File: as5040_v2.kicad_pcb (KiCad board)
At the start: 2 copper layers, 28 x 28 mm, 22 parts, among them J1 Conn_02x05_Odd_Even, J2 Conn_01x05_Male, J3 Conn_01x06_Male, J4 Conn_01x03_Male, U1 AS5045B

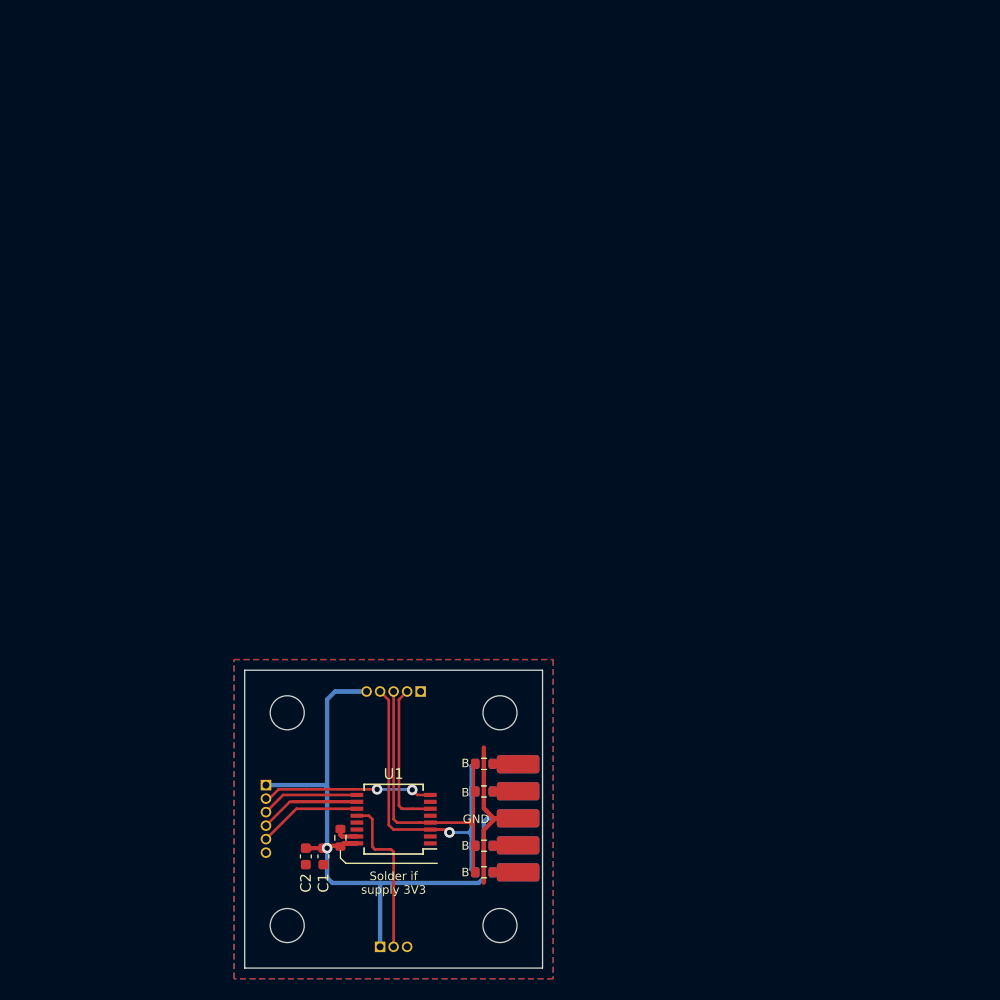
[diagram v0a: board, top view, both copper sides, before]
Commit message: 3x3 grid for cheap pcb production
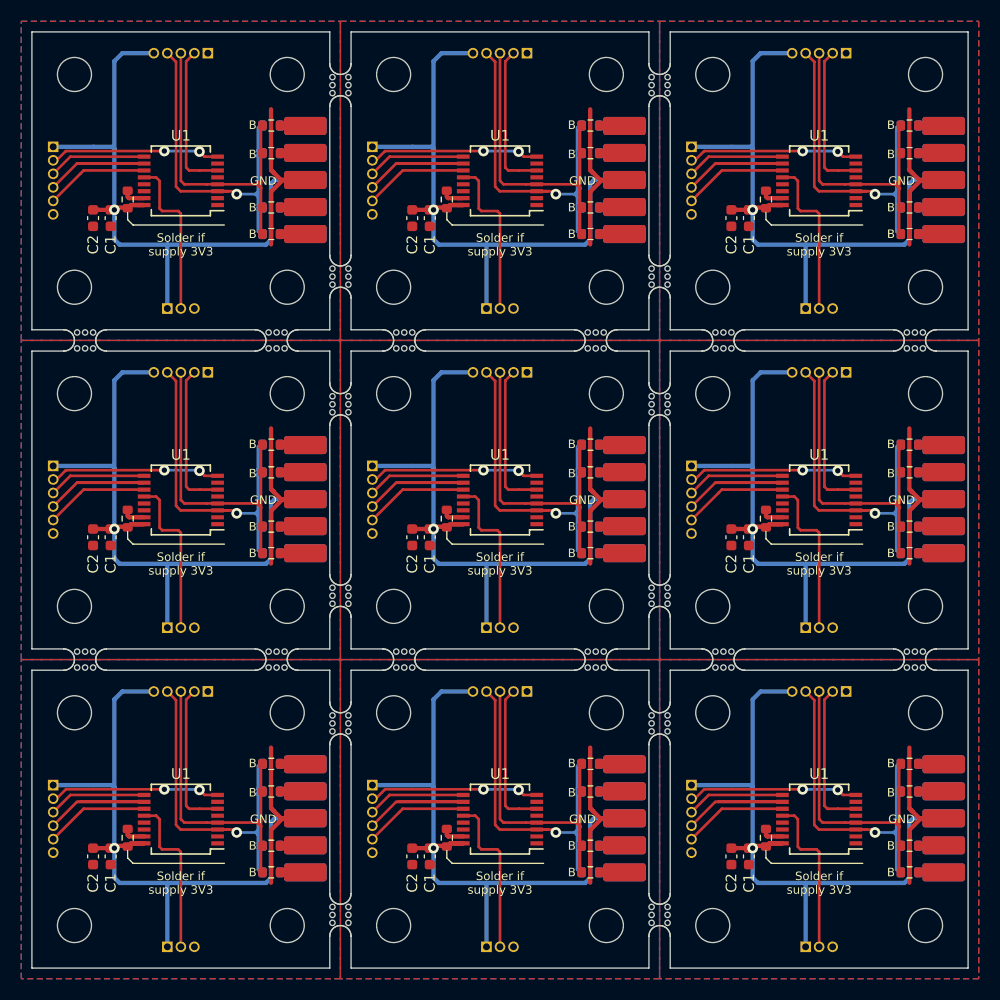
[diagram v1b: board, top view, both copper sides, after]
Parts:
- removed the C1 at (97.4, 139.5)
- removed the C2 at (95.8, 139.5)
- removed the J1 at (113.5, 141.0)
- removed the J2 at (106.5, 124.0)
- removed the J3 at (92.0, 132.8)
- removed the J4 at (102.7, 148.0)
- removed the R1 at (112.5, 133.4)
- removed the R2 at (112.5, 141.0)
- removed the R3 at (112.5, 130.8)
- removed the R4 at (112.5, 138.5)
- removed the R5 at (112.5, 138.5)
- removed the R6 at (112.5, 141.0)
- removed the R7 at (112.5, 130.8)
- removed the R8 at (112.5, 133.4)
- removed the R9 at (99.0, 137.8)
- removed the REF** at (114.0, 146.0)
- removed the REF** at (114.0, 126.0)
- removed the U1 at (104.0, 136.0)
- added C1: 0.1uF, Capacitor_SMD:C_0603_1608Metric, F.Cu at (137.4, 139.5)
- added C1: 0.1uF, Capacitor_SMD:C_0603_1608Metric, F.Cu at (137.4, 79.5)
- added C1: 0.1uF, Capacitor_SMD:C_0603_1608Metric, F.Cu at (137.4, 109.5)
- added C1: 0.1uF, Capacitor_SMD:C_0603_1608Metric, F.Cu at (107.4, 139.5)
- added C1: 0.1uF, Capacitor_SMD:C_0603_1608Metric, F.Cu at (107.4, 79.5)
- added C1: 0.1uF, Capacitor_SMD:C_0603_1608Metric, F.Cu at (107.4, 109.5)
- added C1: 0.1uF, Capacitor_SMD:C_0603_1608Metric, F.Cu at (77.4, 79.5)
- added C1: 0.1uF, Capacitor_SMD:C_0603_1608Metric, F.Cu at (77.4, 109.5)
- added C1: 0.1uF, Capacitor_SMD:C_0603_1608Metric, F.Cu at (77.4, 139.5)
- added C2: 1uF, Capacitor_SMD:C_0603_1608Metric, F.Cu at (135.8, 109.5)
- added C2: 1uF, Capacitor_SMD:C_0603_1608Metric, F.Cu at (135.8, 79.5)
- added C2: 1uF, Capacitor_SMD:C_0603_1608Metric, F.Cu at (135.8, 139.5)
- added C2: 1uF, Capacitor_SMD:C_0603_1608Metric, F.Cu at (105.8, 109.5)
- added C2: 1uF, Capacitor_SMD:C_0603_1608Metric, F.Cu at (105.8, 79.5)
- added C2: 1uF, Capacitor_SMD:C_0603_1608Metric, F.Cu at (105.8, 139.5)
- added C2: 1uF, Capacitor_SMD:C_0603_1608Metric, F.Cu at (75.8, 79.5)
- added C2: 1uF, Capacitor_SMD:C_0603_1608Metric, F.Cu at (75.8, 109.5)
- added C2: 1uF, Capacitor_SMD:C_0603_1608Metric, F.Cu at (75.8, 139.5)
- added G***: LOGO, graphics:progresja_13.4x3.8mm, B.Cu at (143.0, 130.5)
- added G***: LOGO, graphics:progresja_13.4x3.8mm, B.Cu at (143.0, 100.5)
- added G***: LOGO, graphics:progresja_13.4x3.8mm, B.Cu at (143.0, 70.5)
- added G***: LOGO, graphics:progresja_13.4x3.8mm, B.Cu at (113.0, 130.5)
- added G***: LOGO, graphics:progresja_13.4x3.8mm, B.Cu at (113.0, 100.5)
- added G***: LOGO, graphics:progresja_13.4x3.8mm, B.Cu at (113.0, 70.5)
- added G***: LOGO, graphics:progresja_13.4x3.8mm, B.Cu at (83.0, 70.5)
- added G***: LOGO, graphics:progresja_13.4x3.8mm, B.Cu at (83.0, 100.5)
- added J1: Conn_02x05_Odd_Even, as5040_v2:IDC-Header_2x05_P2.54mm_Horizontal, B.Cu at (153.5, 141.0)
- added J1: Conn_02x05_Odd_Even, as5040_v2:IDC-Header_2x05_P2.54mm_Horizontal, B.Cu at (153.5, 111.0)
- added J1: Conn_02x05_Odd_Even, as5040_v2:IDC-Header_2x05_P2.54mm_Horizontal, B.Cu at (153.5, 81.0)
- added J1: Conn_02x05_Odd_Even, as5040_v2:IDC-Header_2x05_P2.54mm_Horizontal, B.Cu at (123.5, 141.0)
- added J1: Conn_02x05_Odd_Even, as5040_v2:IDC-Header_2x05_P2.54mm_Horizontal, B.Cu at (123.5, 111.0)
- added J1: Conn_02x05_Odd_Even, as5040_v2:IDC-Header_2x05_P2.54mm_Horizontal, B.Cu at (123.5, 81.0)
- added J1: Conn_02x05_Odd_Even, as5040_v2:IDC-Header_2x05_P2.54mm_Horizontal, B.Cu at (93.5, 81.0)
- added J1: Conn_02x05_Odd_Even, as5040_v2:IDC-Header_2x05_P2.54mm_Horizontal, B.Cu at (93.5, 111.0)
- added J1: Conn_02x05_Odd_Even, as5040_v2:IDC-Header_2x05_P2.54mm_Horizontal, B.Cu at (93.5, 141.0)
- added J2: Conn_01x05_Male, as5040_v2:PinHeader_1x05_P1.27mm_Horizontal, B.Cu at (146.5, 64.0)
- added J2: Conn_01x05_Male, as5040_v2:PinHeader_1x05_P1.27mm_Horizontal, B.Cu at (146.5, 94.0)
- added J2: Conn_01x05_Male, as5040_v2:PinHeader_1x05_P1.27mm_Horizontal, B.Cu at (146.5, 124.0)
- added J2: Conn_01x05_Male, as5040_v2:PinHeader_1x05_P1.27mm_Horizontal, B.Cu at (116.5, 64.0)
- added J2: Conn_01x05_Male, as5040_v2:PinHeader_1x05_P1.27mm_Horizontal, B.Cu at (116.5, 94.0)
- added J2: Conn_01x05_Male, as5040_v2:PinHeader_1x05_P1.27mm_Horizontal, B.Cu at (116.5, 124.0)
- added J2: Conn_01x05_Male, as5040_v2:PinHeader_1x05_P1.27mm_Horizontal, B.Cu at (86.5, 64.0)
- added J2: Conn_01x05_Male, as5040_v2:PinHeader_1x05_P1.27mm_Horizontal, B.Cu at (86.5, 94.0)
- added J2: Conn_01x05_Male, as5040_v2:PinHeader_1x05_P1.27mm_Horizontal, B.Cu at (86.5, 124.0)
- added J3: Conn_01x06_Male, as5040_v2:PinHeader_1x06_P1.27mm_Horizontal, B.Cu at (132.0, 102.8)
- added J3: Conn_01x06_Male, as5040_v2:PinHeader_1x06_P1.27mm_Horizontal, B.Cu at (132.0, 132.8)
- added J3: Conn_01x06_Male, as5040_v2:PinHeader_1x06_P1.27mm_Horizontal, B.Cu at (132.0, 72.8)
- added J3: Conn_01x06_Male, as5040_v2:PinHeader_1x06_P1.27mm_Horizontal, B.Cu at (102.0, 102.8)
- added J3: Conn_01x06_Male, as5040_v2:PinHeader_1x06_P1.27mm_Horizontal, B.Cu at (102.0, 132.8)
- added J3: Conn_01x06_Male, as5040_v2:PinHeader_1x06_P1.27mm_Horizontal, B.Cu at (102.0, 72.8)
- added J3: Conn_01x06_Male, as5040_v2:PinHeader_1x06_P1.27mm_Horizontal, B.Cu at (72.0, 72.8)
- added J3: Conn_01x06_Male, as5040_v2:PinHeader_1x06_P1.27mm_Horizontal, B.Cu at (72.0, 102.8)
- added J3: Conn_01x06_Male, as5040_v2:PinHeader_1x06_P1.27mm_Horizontal, B.Cu at (72.0, 132.8)
- added J4: Conn_01x03_Male, as5040_v2:PinHeader_1x03_P1.27mm_Horizontal, B.Cu at (142.7, 148.0)
- added J4: Conn_01x03_Male, as5040_v2:PinHeader_1x03_P1.27mm_Horizontal, B.Cu at (142.7, 88.0)
- added J4: Conn_01x03_Male, as5040_v2:PinHeader_1x03_P1.27mm_Horizontal, B.Cu at (142.7, 118.0)
- added J4: Conn_01x03_Male, as5040_v2:PinHeader_1x03_P1.27mm_Horizontal, B.Cu at (112.7, 148.0)
- added J4: Conn_01x03_Male, as5040_v2:PinHeader_1x03_P1.27mm_Horizontal, B.Cu at (112.7, 88.0)
- added J4: Conn_01x03_Male, as5040_v2:PinHeader_1x03_P1.27mm_Horizontal, B.Cu at (112.7, 118.0)
- added J4: Conn_01x03_Male, as5040_v2:PinHeader_1x03_P1.27mm_Horizontal, B.Cu at (82.7, 88.0)
- added J4: Conn_01x03_Male, as5040_v2:PinHeader_1x03_P1.27mm_Horizontal, B.Cu at (82.7, 118.0)
- added J4: Conn_01x03_Male, as5040_v2:PinHeader_1x03_P1.27mm_Horizontal, B.Cu at (82.7, 148.0)
- added R1: 0R, Resistor_SMD:R_0603_1608Metric, B.Cu at (152.5, 103.4)
- added R1: 0R, Resistor_SMD:R_0603_1608Metric, B.Cu at (152.5, 133.4)
- added R1: 0R, Resistor_SMD:R_0603_1608Metric, B.Cu at (152.5, 73.4)
- added R1: 0R, Resistor_SMD:R_0603_1608Metric, B.Cu at (122.5, 103.4)
- added R1: 0R, Resistor_SMD:R_0603_1608Metric, B.Cu at (122.5, 133.4)
- added R1: 0R, Resistor_SMD:R_0603_1608Metric, B.Cu at (122.5, 73.4)
- added R1: 0R, Resistor_SMD:R_0603_1608Metric, B.Cu at (92.5, 73.4)
- added R1: 0R, Resistor_SMD:R_0603_1608Metric, B.Cu at (92.5, 103.4)
- added R1: 0R, Resistor_SMD:R_0603_1608Metric, B.Cu at (92.5, 133.4)
- added R2: 0R, Resistor_SMD:R_0603_1608Metric, B.Cu at (152.5, 141.0)
- added R2: 0R, Resistor_SMD:R_0603_1608Metric, B.Cu at (152.5, 111.0)
- added R2: 0R, Resistor_SMD:R_0603_1608Metric, B.Cu at (152.5, 81.0)
- added R2: 0R, Resistor_SMD:R_0603_1608Metric, B.Cu at (122.5, 141.0)
- added R2: 0R, Resistor_SMD:R_0603_1608Metric, B.Cu at (122.5, 111.0)
- added R2: 0R, Resistor_SMD:R_0603_1608Metric, B.Cu at (122.5, 81.0)
- added R2: 0R, Resistor_SMD:R_0603_1608Metric, B.Cu at (92.5, 81.0)
- added R2: 0R, Resistor_SMD:R_0603_1608Metric, B.Cu at (92.5, 111.0)
- added R2: 0R, Resistor_SMD:R_0603_1608Metric, B.Cu at (92.5, 141.0)
- added R3: 0R, Resistor_SMD:R_0603_1608Metric, B.Cu at (152.5, 130.8)
- added R3: 0R, Resistor_SMD:R_0603_1608Metric, B.Cu at (152.5, 70.8)
- added R3: 0R, Resistor_SMD:R_0603_1608Metric, B.Cu at (152.5, 100.8)
- added R3: 0R, Resistor_SMD:R_0603_1608Metric, B.Cu at (122.5, 130.8)
- added R3: 0R, Resistor_SMD:R_0603_1608Metric, B.Cu at (122.5, 70.8)
- added R3: 0R, Resistor_SMD:R_0603_1608Metric, B.Cu at (122.5, 100.8)
- added R3: 0R, Resistor_SMD:R_0603_1608Metric, B.Cu at (92.5, 70.8)
- added R3: 0R, Resistor_SMD:R_0603_1608Metric, B.Cu at (92.5, 100.8)
- added R3: 0R, Resistor_SMD:R_0603_1608Metric, B.Cu at (92.5, 130.8)
- added R4: 0R, Resistor_SMD:R_0603_1608Metric, B.Cu at (152.5, 78.5)
- added R4: 0R, Resistor_SMD:R_0603_1608Metric, B.Cu at (152.5, 138.5)
- added R4: 0R, Resistor_SMD:R_0603_1608Metric, B.Cu at (152.5, 108.5)
- added R4: 0R, Resistor_SMD:R_0603_1608Metric, B.Cu at (122.5, 78.5)
- added R4: 0R, Resistor_SMD:R_0603_1608Metric, B.Cu at (122.5, 138.5)
- added R4: 0R, Resistor_SMD:R_0603_1608Metric, B.Cu at (122.5, 108.5)
- added R4: 0R, Resistor_SMD:R_0603_1608Metric, B.Cu at (92.5, 78.5)
- added R4: 0R, Resistor_SMD:R_0603_1608Metric, B.Cu at (92.5, 108.5)
- added R4: 0R, Resistor_SMD:R_0603_1608Metric, B.Cu at (92.5, 138.5)
- added R5: 0R, Resistor_SMD:R_0603_1608Metric, F.Cu at (152.5, 138.5)
- added R5: 0R, Resistor_SMD:R_0603_1608Metric, F.Cu at (152.5, 108.5)
- added R5: 0R, Resistor_SMD:R_0603_1608Metric, F.Cu at (152.5, 78.5)
- added R5: 0R, Resistor_SMD:R_0603_1608Metric, F.Cu at (122.5, 138.5)
- added R5: 0R, Resistor_SMD:R_0603_1608Metric, F.Cu at (122.5, 108.5)
- added R5: 0R, Resistor_SMD:R_0603_1608Metric, F.Cu at (122.5, 78.5)
- added R5: 0R, Resistor_SMD:R_0603_1608Metric, F.Cu at (92.5, 78.5)
- added R5: 0R, Resistor_SMD:R_0603_1608Metric, F.Cu at (92.5, 108.5)
- added R5: 0R, Resistor_SMD:R_0603_1608Metric, F.Cu at (92.5, 138.5)
- added R6: 0R, Resistor_SMD:R_0603_1608Metric, F.Cu at (152.5, 141.0)
- added R6: 0R, Resistor_SMD:R_0603_1608Metric, F.Cu at (152.5, 111.0)
- added R6: 0R, Resistor_SMD:R_0603_1608Metric, F.Cu at (152.5, 81.0)
- added R6: 0R, Resistor_SMD:R_0603_1608Metric, F.Cu at (122.5, 141.0)
- added R6: 0R, Resistor_SMD:R_0603_1608Metric, F.Cu at (122.5, 111.0)
- added R6: 0R, Resistor_SMD:R_0603_1608Metric, F.Cu at (122.5, 81.0)
- added R6: 0R, Resistor_SMD:R_0603_1608Metric, F.Cu at (92.5, 81.0)
- added R6: 0R, Resistor_SMD:R_0603_1608Metric, F.Cu at (92.5, 111.0)
- added R6: 0R, Resistor_SMD:R_0603_1608Metric, F.Cu at (92.5, 141.0)
- added R7: 0R, Resistor_SMD:R_0603_1608Metric, F.Cu at (152.5, 130.8)
- added R7: 0R, Resistor_SMD:R_0603_1608Metric, F.Cu at (152.5, 100.8)
- added R7: 0R, Resistor_SMD:R_0603_1608Metric, F.Cu at (152.5, 70.8)
- added R7: 0R, Resistor_SMD:R_0603_1608Metric, F.Cu at (122.5, 130.8)
- added R7: 0R, Resistor_SMD:R_0603_1608Metric, F.Cu at (122.5, 100.8)
- added R7: 0R, Resistor_SMD:R_0603_1608Metric, F.Cu at (122.5, 70.8)
- added R7: 0R, Resistor_SMD:R_0603_1608Metric, F.Cu at (92.5, 70.8)
- added R7: 0R, Resistor_SMD:R_0603_1608Metric, F.Cu at (92.5, 100.8)
- added R7: 0R, Resistor_SMD:R_0603_1608Metric, F.Cu at (92.5, 130.8)
- added R8: 0R, Resistor_SMD:R_0603_1608Metric, F.Cu at (152.5, 103.4)
- added R8: 0R, Resistor_SMD:R_0603_1608Metric, F.Cu at (152.5, 133.4)
- added R8: 0R, Resistor_SMD:R_0603_1608Metric, F.Cu at (152.5, 73.4)
- added R8: 0R, Resistor_SMD:R_0603_1608Metric, F.Cu at (122.5, 103.4)
- added R8: 0R, Resistor_SMD:R_0603_1608Metric, F.Cu at (122.5, 133.4)
- added R8: 0R, Resistor_SMD:R_0603_1608Metric, F.Cu at (122.5, 73.4)
- added R8: 0R, Resistor_SMD:R_0603_1608Metric, F.Cu at (92.5, 73.4)
- added R8: 0R, Resistor_SMD:R_0603_1608Metric, F.Cu at (92.5, 103.4)
- added R8: 0R, Resistor_SMD:R_0603_1608Metric, F.Cu at (92.5, 133.4)
- added R9: 0R, Resistor_SMD:R_0603_1608Metric, F.Cu at (139.0, 107.8)
- added R9: 0R, Resistor_SMD:R_0603_1608Metric, F.Cu at (139.0, 137.8)
- added R9: 0R, Resistor_SMD:R_0603_1608Metric, F.Cu at (139.0, 77.8)
- added R9: 0R, Resistor_SMD:R_0603_1608Metric, F.Cu at (109.0, 107.8)
- added R9: 0R, Resistor_SMD:R_0603_1608Metric, F.Cu at (109.0, 137.8)
- added R9: 0R, Resistor_SMD:R_0603_1608Metric, F.Cu at (109.0, 77.8)
- added R9: 0R, Resistor_SMD:R_0603_1608Metric, F.Cu at (79.0, 77.8)
- added R9: 0R, Resistor_SMD:R_0603_1608Metric, F.Cu at (79.0, 107.8)
- added R9: 0R, Resistor_SMD:R_0603_1608Metric, F.Cu at (79.0, 137.8)
- added REF**: OSHW-Logo_5.7x6mm_SilkScreen, Symbol:OSHW-Logo_5.7x6mm_SilkScreen, B.Cu at (140.0, 140.5)
- added REF**: MountingHole_3.2mm_M3, MountingHole:MountingHole_3.2mm_M3, F.Cu at (134.0, 86.0)
- added REF**: MountingHole_3.2mm_M3, MountingHole:MountingHole_3.2mm_M3, F.Cu at (154.0, 96.0)
- added REF**: MountingHole_3.2mm_M3, MountingHole:MountingHole_3.2mm_M3, F.Cu at (134.0, 116.0)
- added REF**: MountingHole_3.2mm_M3, MountingHole:MountingHole_3.2mm_M3, F.Cu at (154.0, 116.0)
- added REF**: OSHW-Logo_5.7x6mm_SilkScreen, Symbol:OSHW-Logo_5.7x6mm_SilkScreen, B.Cu at (140.0, 110.5)
- added REF**: MountingHole_3.2mm_M3, MountingHole:MountingHole_3.2mm_M3, F.Cu at (154.0, 86.0)
- added REF**: OSHW-Logo_5.7x6mm_SilkScreen, Symbol:OSHW-Logo_5.7x6mm_SilkScreen, B.Cu at (110.0, 140.5)
- added REF**: MountingHole_3.2mm_M3, MountingHole:MountingHole_3.2mm_M3, F.Cu at (104.0, 96.0)
- added REF**: MountingHole_3.2mm_M3, MountingHole:MountingHole_3.2mm_M3, F.Cu at (124.0, 126.0)
- added REF**: MountingHole_3.2mm_M3, MountingHole:MountingHole_3.2mm_M3, F.Cu at (104.0, 126.0)
- added REF**: MountingHole_3.2mm_M3, MountingHole:MountingHole_3.2mm_M3, F.Cu at (134.0, 96.0)
- added REF**: MountingHole_3.2mm_M3, MountingHole:MountingHole_3.2mm_M3, F.Cu at (124.0, 146.0)
- added REF**: MountingHole_3.2mm_M3, MountingHole:MountingHole_3.2mm_M3, F.Cu at (104.0, 146.0)
- added REF**: MountingHole_3.2mm_M3, MountingHole:MountingHole_3.2mm_M3, F.Cu at (124.0, 66.0)
- added REF**: MountingHole_3.2mm_M3, MountingHole:MountingHole_3.2mm_M3, F.Cu at (104.0, 66.0)
- added REF**: OSHW-Logo_5.7x6mm_SilkScreen, Symbol:OSHW-Logo_5.7x6mm_SilkScreen, B.Cu at (110.0, 80.5)
- added REF**: MountingHole_3.2mm_M3, MountingHole:MountingHole_3.2mm_M3, F.Cu at (104.0, 86.0)
- added REF**: MountingHole_3.2mm_M3, MountingHole:MountingHole_3.2mm_M3, F.Cu at (124.0, 96.0)
- added REF**: MountingHole_3.2mm_M3, MountingHole:MountingHole_3.2mm_M3, F.Cu at (104.0, 116.0)
- added REF**: MountingHole_3.2mm_M3, MountingHole:MountingHole_3.2mm_M3, F.Cu at (124.0, 116.0)
- added REF**: OSHW-Logo_5.7x6mm_SilkScreen, Symbol:OSHW-Logo_5.7x6mm_SilkScreen, B.Cu at (110.0, 110.5)
- added REF**: MountingHole_3.2mm_M3, MountingHole:MountingHole_3.2mm_M3, F.Cu at (154.0, 126.0)
- added REF**: MountingHole_3.2mm_M3, MountingHole:MountingHole_3.2mm_M3, F.Cu at (124.0, 86.0)
- added REF**: OSHW-Logo_5.7x6mm_SilkScreen, Symbol:OSHW-Logo_5.7x6mm_SilkScreen, B.Cu at (80.0, 80.5)
- added REF**: MountingHole_3.2mm_M3, MountingHole:MountingHole_3.2mm_M3, F.Cu at (94.0, 66.0)
- added REF**: MountingHole_3.2mm_M3, MountingHole:MountingHole_3.2mm_M3, F.Cu at (74.0, 66.0)
- added REF**: MountingHole_3.2mm_M3, MountingHole:MountingHole_3.2mm_M3, F.Cu at (94.0, 86.0)
- added REF**: MountingHole_3.2mm_M3, MountingHole:MountingHole_3.2mm_M3, F.Cu at (74.0, 86.0)
- added REF**: OSHW-Logo_5.7x6mm_SilkScreen, Symbol:OSHW-Logo_5.7x6mm_SilkScreen, B.Cu at (80.0, 110.5)
- added REF**: MountingHole_3.2mm_M3, MountingHole:MountingHole_3.2mm_M3, F.Cu at (94.0, 96.0)
- added REF**: MountingHole_3.2mm_M3, MountingHole:MountingHole_3.2mm_M3, F.Cu at (74.0, 96.0)
- added REF**: MountingHole_3.2mm_M3, MountingHole:MountingHole_3.2mm_M3, F.Cu at (94.0, 116.0)
- added REF**: MountingHole_3.2mm_M3, MountingHole:MountingHole_3.2mm_M3, F.Cu at (134.0, 126.0)
- added REF**: MountingHole_3.2mm_M3, MountingHole:MountingHole_3.2mm_M3, F.Cu at (74.0, 116.0)
- added REF**: MountingHole_3.2mm_M3, MountingHole:MountingHole_3.2mm_M3, F.Cu at (74.0, 146.0)
- added REF**: MountingHole_3.2mm_M3, MountingHole:MountingHole_3.2mm_M3, F.Cu at (74.0, 126.0)
- added REF**: MountingHole_3.2mm_M3, MountingHole:MountingHole_3.2mm_M3, F.Cu at (154.0, 146.0)
- added REF**: MountingHole_3.2mm_M3, MountingHole:MountingHole_3.2mm_M3, F.Cu at (134.0, 146.0)
- added REF**: MountingHole_3.2mm_M3, MountingHole:MountingHole_3.2mm_M3, F.Cu at (154.0, 66.0)
- added REF**: MountingHole_3.2mm_M3, MountingHole:MountingHole_3.2mm_M3, F.Cu at (134.0, 66.0)
- added REF**: OSHW-Logo_5.7x6mm_SilkScreen, Symbol:OSHW-Logo_5.7x6mm_SilkScreen, B.Cu at (140.0, 80.5)
- added U1: AS5045B, Package_SO:SSOP-16_5.3x6.2mm_P0.65mm, F.Cu at (144.0, 136.0)
- added U1: AS5045B, Package_SO:SSOP-16_5.3x6.2mm_P0.65mm, F.Cu at (144.0, 76.0)
- added U1: AS5045B, Package_SO:SSOP-16_5.3x6.2mm_P0.65mm, F.Cu at (144.0, 106.0)
- added U1: AS5045B, Package_SO:SSOP-16_5.3x6.2mm_P0.65mm, F.Cu at (114.0, 136.0)
- added U1: AS5045B, Package_SO:SSOP-16_5.3x6.2mm_P0.65mm, F.Cu at (114.0, 76.0)
- added U1: AS5045B, Package_SO:SSOP-16_5.3x6.2mm_P0.65mm, F.Cu at (114.0, 106.0)
- added U1: AS5045B, Package_SO:SSOP-16_5.3x6.2mm_P0.65mm, F.Cu at (84.0, 76.0)
- added U1: AS5045B, Package_SO:SSOP-16_5.3x6.2mm_P0.65mm, F.Cu at (84.0, 106.0)
- added U1: AS5045B, Package_SO:SSOP-16_5.3x6.2mm_P0.65mm, F.Cu at (84.0, 136.0)
- added mouse-bite-2mm-slot: VAL**, as5040_v2:mouse-bite-2mm-slot, F.Cu at (129.0, 145.0)
- added mouse-bite-2mm-slot: VAL**, as5040_v2:mouse-bite-2mm-slot, F.Cu at (129.0, 67.0)
- added mouse-bite-2mm-slot: VAL**, as5040_v2:mouse-bite-2mm-slot, F.Cu at (99.0, 85.0)
- added mouse-bite-2mm-slot: VAL**, as5040_v2:mouse-bite-2mm-slot, F.Cu at (99.0, 67.0)
- added mouse-bite-2mm-slot: VAL**, as5040_v2:mouse-bite-2mm-slot, F.Cu at (135.0, 121.0)
- added mouse-bite-2mm-slot: VAL**, as5040_v2:mouse-bite-2mm-slot, F.Cu at (153.0, 121.0)
- added mouse-bite-2mm-slot: VAL**, as5040_v2:mouse-bite-2mm-slot, F.Cu at (135.0, 91.0)
- added mouse-bite-2mm-slot: VAL**, as5040_v2:mouse-bite-2mm-slot, F.Cu at (153.0, 91.0)
- added mouse-bite-2mm-slot: VAL**, as5040_v2:mouse-bite-2mm-slot, F.Cu at (105.0, 91.0)
- added mouse-bite-2mm-slot: VAL**, as5040_v2:mouse-bite-2mm-slot, F.Cu at (123.0, 91.0)
- added mouse-bite-2mm-slot: VAL**, as5040_v2:mouse-bite-2mm-slot, F.Cu at (105.0, 121.0)
- added mouse-bite-2mm-slot: VAL**, as5040_v2:mouse-bite-2mm-slot, F.Cu at (129.0, 127.0)
- added mouse-bite-2mm-slot: VAL**, as5040_v2:mouse-bite-2mm-slot, F.Cu at (123.0, 121.0)
- added mouse-bite-2mm-slot: VAL**, as5040_v2:mouse-bite-2mm-slot, F.Cu at (75.0, 121.0)
- added mouse-bite-2mm-slot: VAL**, as5040_v2:mouse-bite-2mm-slot, F.Cu at (93.0, 121.0)
- added mouse-bite-2mm-slot: VAL**, as5040_v2:mouse-bite-2mm-slot, F.Cu at (75.0, 91.0)
- added mouse-bite-2mm-slot: VAL**, as5040_v2:mouse-bite-2mm-slot, F.Cu at (93.0, 91.0)
- added mouse-bite-2mm-slot: VAL**, as5040_v2:mouse-bite-2mm-slot, F.Cu at (99.0, 145.0)
- added mouse-bite-2mm-slot: VAL**, as5040_v2:mouse-bite-2mm-slot, F.Cu at (99.0, 127.0)
- added mouse-bite-2mm-slot: VAL**, as5040_v2:mouse-bite-2mm-slot, F.Cu at (129.0, 115.0)
- added mouse-bite-2mm-slot: VAL**, as5040_v2:mouse-bite-2mm-slot, F.Cu at (129.0, 97.0)
- added mouse-bite-2mm-slot: VAL**, as5040_v2:mouse-bite-2mm-slot, F.Cu at (99.0, 115.0)
- added mouse-bite-2mm-slot: VAL**, as5040_v2:mouse-bite-2mm-slot, F.Cu at (99.0, 97.0)
- added mouse-bite-2mm-slot: VAL**, as5040_v2:mouse-bite-2mm-slot, F.Cu at (129.0, 85.0)
- moved G*** 20.0 mm to (83.0, 130.5)
- moved REF** 20.0 mm to (80.0, 140.5)
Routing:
- net (no net): track 0.00 -> 1988.2 mm, vias 0 -> 32
- added copper zone on B.Cu, net (none)
- added copper zone on F.Cu, net (none)
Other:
- board size 28 x 28 mm -> 88 x 88 mm
